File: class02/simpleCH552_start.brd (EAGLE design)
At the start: 40.6 x 12 mm, 6 parts, among them U1 CH552G, X1 USBPCB

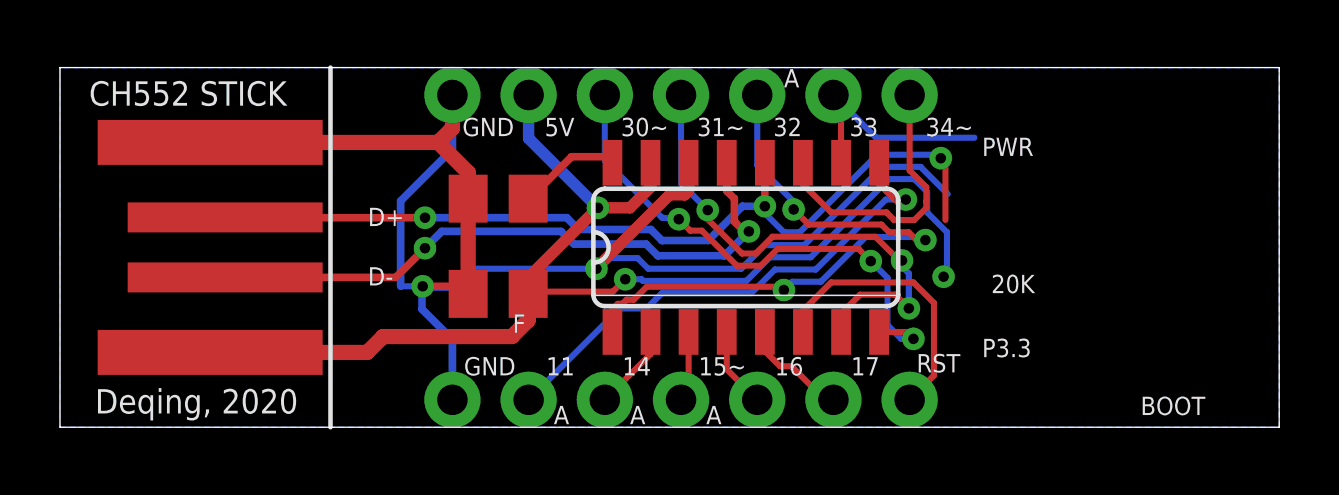
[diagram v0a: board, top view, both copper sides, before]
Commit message: update to USB shell model
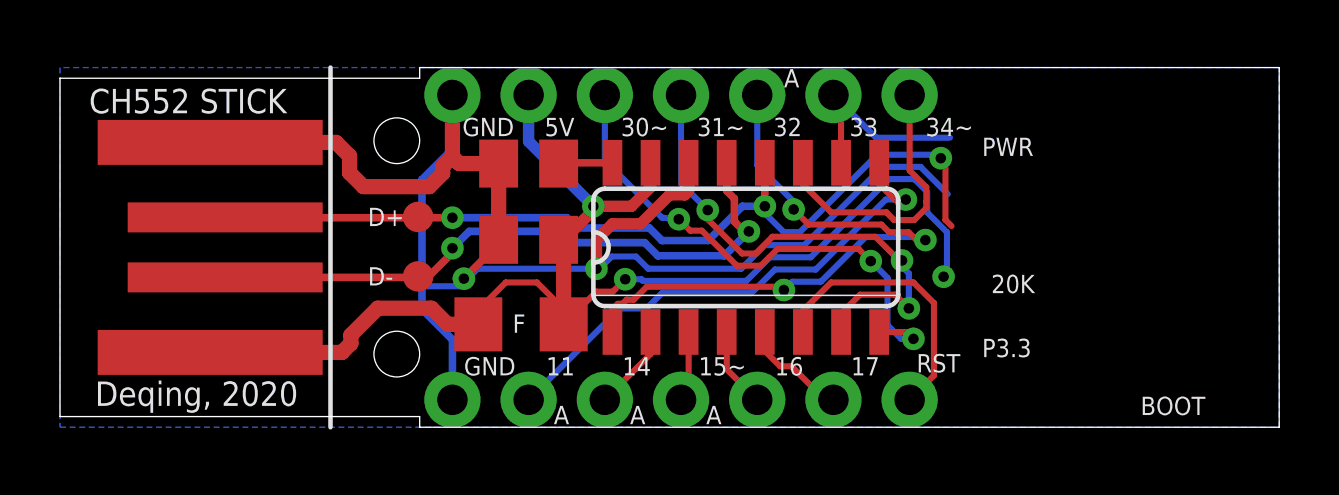
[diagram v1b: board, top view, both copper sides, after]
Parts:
- added F1: (no value), adafruit:R1206
- added TP1, TP2: TEST-POINT3X4, SparkFun-Connectors:PAD.03X.04
- moved C1 2.07 mm to (15.6, 6.25)
- moved C2 1.55 mm to (15.6, 8.79)
- renumbered U1 to U2
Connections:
- net +5V: now also F1.1, F1.2
- net USB_D+: now also TP2.P$1
- net USB_D-: now also TP1.P$1
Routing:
- net +5V: track 41.6 -> 43.8 mm
- net 3.3V: track 3.46 -> 1.80 mm
- net USB_D+: track 29.8 -> 31.3 mm
- net P3.3: track 7.65 -> 6.84 mm
- net GND: track 53.5 -> 54.1 mm
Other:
- outline, holes or cut-outs redrawn
- board text added: "Deqing Sun, 2020 Try Ch55xduino with this board"
- board text added: "Deqing Sun, 2022 Prototyping Electronic Devices"
- board text removed: "Deqing Sun, 2020 Prototyping Electronic Devices"
